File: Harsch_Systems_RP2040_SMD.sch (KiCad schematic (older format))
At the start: 53 parts, among them J1 Jack-DC, J3 Conn_01x08_Female, J4 Conn_01x08_Female, J5 Conn_01x04_Female, J6 Conn_01x06_Female, J7 USB_A, J8 DEBUG, SW1 SW_MEC_5E, U1 XC6210B332MR, U11 TPS56339DDC, U3 RP2040, U4 W25Q32JVSSIQ_TR, Y1 12MHz

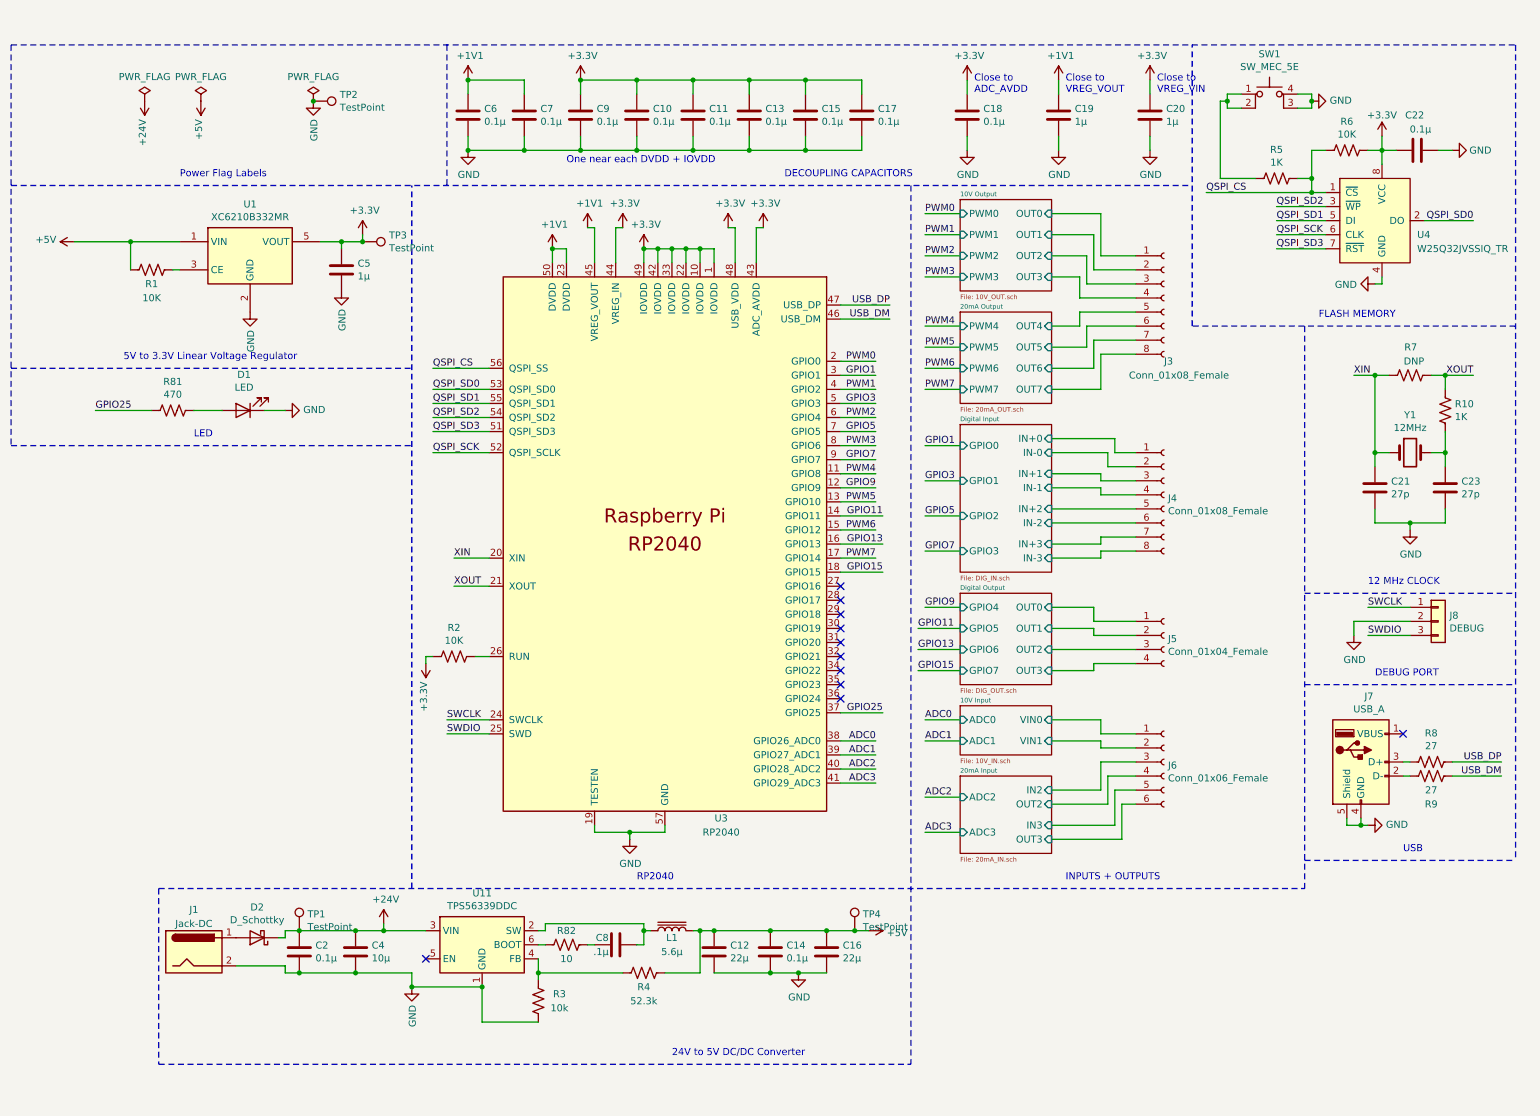
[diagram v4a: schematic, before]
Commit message: Everything but the 24V output is routed
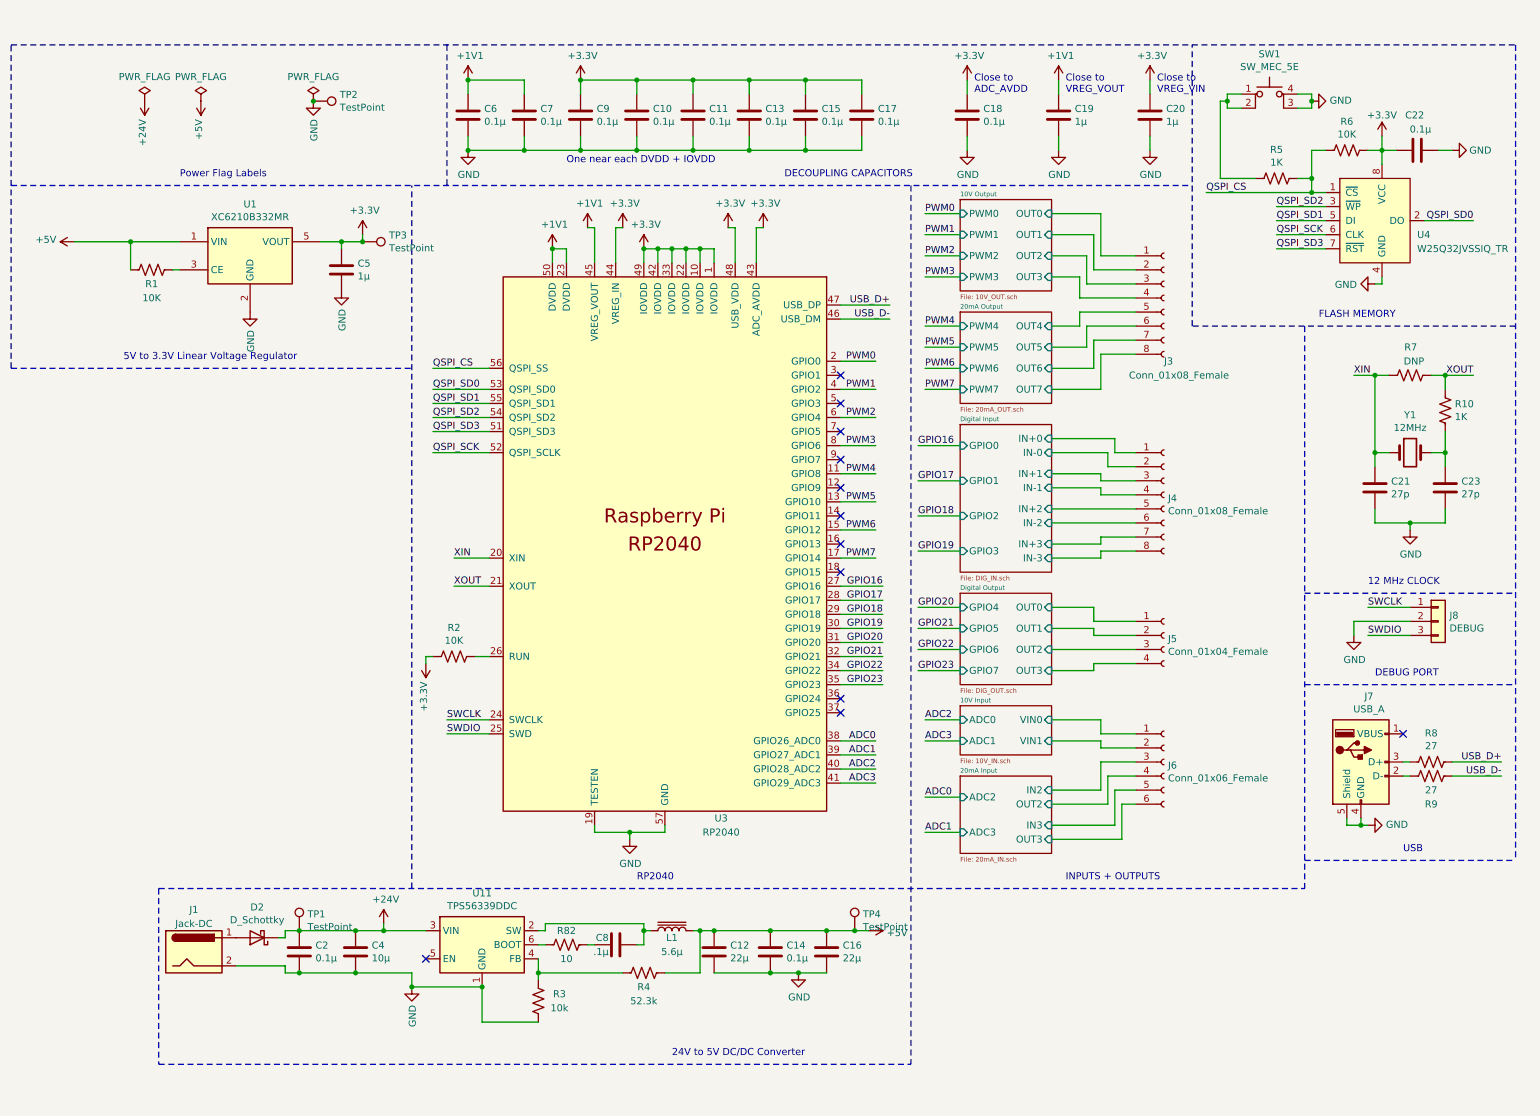
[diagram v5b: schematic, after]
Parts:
- removed D1: LED, LED_SMD:LED_0805_2012Metric, symbol Device:LED
- removed R81: 470, Resistor_SMD:R_0805_2012Metric, symbol Device:R_US
- C10, C11, C13, C15, C17, C6, C7, C9: footprint Capacitor_SMD:C_0402_1005Metric_Pad0.74x0.62mm_HandSolder -> Capacitor_SMD:C_0603_1608Metric
- C19, C20: footprint Capacitor_SMD:C_0805_2012Metric -> Capacitor_SMD:C_0603_1608Metric
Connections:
- net GPIO16: now reaches U3.27 (GPIO16)
- net GPIO17: now reaches U3.28 (GPIO17)
- net GPIO18: now reaches U3.29 (GPIO18)
- net GPIO19: now reaches U3.30 (GPIO19)
- net GPIO20: now reaches U3.31 (GPIO20)
- net GPIO21: now reaches U3.32 (GPIO21)
- net GPIO22: now reaches U3.34 (GPIO22)
- net GPIO23: now reaches U3.35 (GPIO23)
- net GPIO1: no longer names the net of U3.3 (GPIO1)
- net GPIO11: no longer names the net of U3.14 (GPIO11)
- net GPIO13: no longer names the net of U3.16 (GPIO13)
- net GPIO15: no longer names the net of U3.18 (GPIO15)
- net GPIO25: no longer names the net of U3.37 (GPIO25)
- net GPIO3: no longer names the net of U3.5 (GPIO3)
- net GPIO5: no longer names the net of U3.7 (GPIO5)
- net GPIO7: no longer names the net of U3.9 (GPIO7)
- net GPIO9: no longer names the net of U3.12 (GPIO9)
- net USB_DM renamed USB_D-
- net USB_DP renamed USB_D+
- no-connect marks 11 -> 12
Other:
- note removed: "LED"
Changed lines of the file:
@@
 F 0 "C9" H 4665 1046 50  0000 L CNN
 F 1 "0.1μ" H 4665 955 50  0000 L CNN
-F 2 "Capacitor_SMD:C_0402_1005Metric_Pad0.74x0.62mm_HandSolder" H 4588 850 50  0001 C CNN
+F 2 "Capacitor_SMD:C_0603_1608Metric" H 4588 850 50  0001 C CNN
 F 3 "~" H 4550 1000 50  0001 C CNN
 	1    4550 1000
@@
 F 0 "C10" H 5065 1046 50  0000 L CNN
 F 1 "0.1μ" H 5065 955 50  0000 L CNN
-F 2 "Capacitor_SMD:C_0402_1005Metric_Pad0.74x0.62mm_HandSolder" H 4988 850 50  0001 C CNN
+F 2 "Capacitor_SMD:C_0603_1608Metric" H 4988 850 50  0001 C CNN
 F 3 "~" H 4950 1000 50  0001 C CNN
 	1    4950 1000
@@
 F 0 "C11" H 5465 1046 50  0000 L CNN
 F 1 "0.1μ" H 5465 955 50  0000 L CNN
-F 2 "Capacitor_SMD:C_0402_1005Metric_Pad0.74x0.62mm_HandSolder" H 5388 850 50  0001 C CNN
+F 2 "Capacitor_SMD:C_0603_1608Metric" H 5388 850 50  0001 C CNN
 F 3 "~" H 5350 1000 50  0001 C CNN
 	1    5350 1000
@@
 F 0 "C13" H 5865 1046 50  0000 L CNN
 F 1 "0.1μ" H 5865 955 50  0000 L CNN
-F 2 "Capacitor_SMD:C_0402_1005Metric_Pad0.74x0.62mm_HandSolder" H 5788 850 50  0001 C CNN
+F 2 "Capacitor_SMD:C_0603_1608Metric" H 5788 850 50  0001 C CNN
 F 3 "~" H 5750 1000 50  0001 C CNN
 	1    5750 1000
@@
 F 0 "C15" H 6265 1046 50  0000 L CNN
 F 1 "0.1μ" H 6265 955 50  0000 L CNN
-F 2 "Capacitor_SMD:C_0402_1005Metric_Pad0.74x0.62mm_HandSolder" H 6188 850 50  0001 C CNN
+F 2 "Capacitor_SMD:C_0603_1608Metric" H 6188 850 50  0001 C CNN
 F 3 "~" H 6150 1000 50  0001 C CNN
 	1    6150 1000
@@
 F 0 "C17" H 6665 1046 50  0000 L CNN
 F 1 "0.1μ" H 6665 955 50  0000 L CNN
-F 2 "Capacitor_SMD:C_0402_1005Metric_Pad0.74x0.62mm_HandSolder" H 6588 850 50  0001 C CNN
+F 2 "Capacitor_SMD:C_0603_1608Metric" H 6588 850 50  0001 C CNN
 F 3 "~" H 6550 1000 50  0001 C CNN
 	1    6550 1000
@@
 Connection ~ 10100 6050
 Text Label 11100 5600 2    50   ~ 0
-USB_DP
+USB_D+
 Text Label 11100 5700 2    50   ~ 0
-USB_DM
+USB_D-
 $Comp
 L Device:R_US R8
@@
 	10750 5700 11100 5700
 Text Label 6750 2450 2    50   ~ 0
-USB_DM
+USB_D-
 Text Label 6750 2350 2    50   ~ 0
-USB_DP
+USB_D+
 Wire Wire Line
 	6400 2350 6750 2350
@@
 F 0 "C6" H 3865 1046 50  0000 L CNN
 F 1 "0.1μ" H 3865 955 50  0000 L CNN
-F 2 "Capacitor_SMD:C_0402_1005Metric_Pad0.74x0.62mm_HandSolder" H 3788 850 50  0001 C CNN
+F 2 "Capacitor_SMD:C_0603_1608Metric" H 3788 850 50  0001 C CNN
 F 3 "~" H 3750 1000 50  0001 C CNN
 	1    3750 1000
@@
 F 0 "C7" H 4265 1046 50  0000 L CNN
 F 1 "0.1μ" H 4265 955 50  0000 L CNN
-F 2 "Capacitor_SMD:C_0402_1005Metric_Pad0.74x0.62mm_HandSolder" H 4188 850 50  0001 C CNN
+F 2 "Capacitor_SMD:C_0603_1608Metric" H 4188 850 50  0001 C CNN
 F 3 "~" H 4150 1000 50  0001 C CNN
 	1    4150 1000
@@
 F 0 "C19" H 8065 1046 50  0000 L CNN
 F 1 "1μ" H 8065 955 50  0000 L CNN
-F 2 "Capacitor_SMD:C_0805_2012Metric" H 7988 850 50  0001 C CNN
+F 2 "Capacitor_SMD:C_0603_1608Metric" H 7988 850 50  0001 C CNN
 F 3 "~" H 7950 1000 50  0001 C CNN
 	1    7950 1000
@@
 F 0 "C20" H 8715 1046 50  0000 L CNN
 F 1 "1μ" H 8715 955 50  0000 L CNN
-F 2 "Capacitor_SMD:C_0805_2012Metric" H 8638 850 50  0001 C CNN
+F 2 "Capacitor_SMD:C_0603_1608Metric" H 8638 850 50  0001 C CNN
 F 3 "~" H 8600 1000 50  0001 C CNN
 	1    8600 1000
@@
 Wire Wire Line
 	8400 5900 8500 5900
-NoConn ~ 6400 4350
-NoConn ~ 6400 4450
-NoConn ~ 6400 4550
-NoConn ~ 6400 4650
-NoConn ~ 6400 4750
-NoConn ~ 6400 4850
-NoConn ~ 6400 4950
-NoConn ~ 6400 5050
 NoConn ~ 6400 5150
 $Comp
@@
 Wire Wire Line
 	6400 4150 6650 4150
-Text Label 6650 2850 2    50   ~ 0
-GPIO1
-Text Label 6650 3050 2    50   ~ 0
-GPIO3
-Text Label 6650 3250 2    50   ~ 0
-GPIO5
-Text Label 6650 3450 2    50   ~ 0
-GPIO7
-Text Label 6650 3650 2    50   ~ 0
-GPIO9
-Text Label 6700 3850 2    50   ~ 0
-GPIO11
-Text Label 6700 4050 2    50   ~ 0
-GPIO13
-Text Label 6700 4250 2    50   ~ 0
-GPIO15
-Wire Wire Line
-	6400 2850 6650 2850
-Wire Wire Line
-	6400 3050 6650 3050
-Wire Wire Line
-	6400 3250 6650 3250
-Wire Wire Line
-	6400 3450 6650 3450
-Wire Wire Line
-	6400 3850 6700 3850
-Wire Wire Line
-	6400 4050 6700 4050
-Wire Wire Line
-	6400 4250 6700 4250
-Wire Wire Line
-	6400 3650 6650 3650
+Text Label 6700 5050 2    50   ~ 0
+GPIO23
+Text Label 6700 4350 2    50   ~ 0
+GPIO16
+Text Label 6700 4450 2    50   ~ 0
+GPIO17
+Text Label 6700 4550 2    50   ~ 0
+GPIO18
+Text Label 6700 4650 2    50   ~ 0
+GPIO19
+Text Label 6700 4750 2    50   ~ 0
+GPIO20
+Text Label 6700 4850 2    50   ~ 0
+GPIO21
+Text Label 6700 4950 2    50   ~ 0
+GPIO22
+Wire Wire Line
+	6400 4750 6700 4750
+Wire Wire Line
+	6400 4850 6700 4850
+Wire Wire Line
+	6400 4950 6700 4950
 Text Label 7000 1700 0    50   ~ 0
 PWM0
@@
 Text Label 7000 2950 0    50   ~ 0
 PWM7
-Text Label 7000 3350 0    50   ~ 0
-GPIO1
-Text Label 7000 3600 0    50   ~ 0
-GPIO3
-Text Label 7000 3850 0    50   ~ 0
-GPIO5
-Text Label 7000 4100 0    50   ~ 0
-GPIO7
-Text Label 7000 4500 0    50   ~ 0
-GPIO9
+Text Label 6950 4950 0    50   ~ 0
+GPIO23
+Text Label 6950 3350 0    50   ~ 0
+GPIO16
+Text Label 6950 3600 0    50   ~ 0
+GPIO17
+Text Label 6950 3850 0    50   ~ 0
+GPIO18
+Text Label 6950 4100 0    50   ~ 0
+GPIO19
+Text Label 6950 4500 0    50   ~ 0
+GPIO20
 Text Label 6950 4650 0    50   ~ 0
-GPIO11
+GPIO21
 Text Label 6950 4800 0    50   ~ 0
-GPIO13
-Text Label 6950 4950 0    50   ~ 0
-GPIO15
+GPIO22
 Wire Wire Line
 	7000 1700 7250 1700
@@
 	7000 2950 7250 2950
 Wire Wire Line
-	7000 3350 7250 3350
-Wire Wire Line
-	7000 3600 7250 3600
-Wire Wire Line
-	7000 3850 7250 3850
-Wire Wire Line
-	7000 4100 7250 4100
-Wire Wire Line
-	7000 4500 7250 4500
+	6950 4500 7250 4500
 Wire Wire Line
 	6950 4650 7250 4650
 Wire Wire Line
 	6950 4800 7250 4800
-Wire Wire Line
-	6950 4950 7250 4950
 Text Label 6650 5450 2    50   ~ 0
 ADC0
@@
 Text Label 6650 5750 2    50   ~ 0
 ADC3
+Text Label 7000 5850 0    50   ~ 0
+ADC0
+Text Label 7000 6100 0    50   ~ 0
+ADC1
 Text Label 7000 5300 0    50   ~ 0
-ADC0
+ADC2
 Text Label 7000 5450 0    50   ~ 0
-ADC1
-Text Label 7000 5850 0    50   ~ 0
-ADC2
-Text Label 7000 6100 0    50   ~ 0
 ADC3
 Wire Wire Line
@@
 Text Notes 1300 2750 0    50   ~ 0
 5V to 3.3V Linear Voltage Regulator
-Wire Wire Line
-	6400 5250 6700 5250
-Text Label 6700 5250 2    50   ~ 0
-GPIO25
-$Comp
-L Device:LED D1
-U 1 1 61F17205
-P 2150 3100
-F 0 "D1" H 2143 2845 50  0000 C CNN
-F 1 "LED" H 2143 2936 50  0000 C CNN
-F 2 "LED_SMD:LED_0805_2012Metric" H 2150 3100 50  0001 C CNN
-F 3 "~" H 2150 3100 50  0001 C CNN
-	1    2150 3100
-	-1   0    0    1
-$EndComp
-$Comp
-L Device:R_US R81
-U 1 1 61F18BAC
-P 1650 3100
-F 0 "R81" V 1445 3100 50  0000 C CNN
-F 1 "470" V 1536 3100 50  0000 C CNN
-F 2 "Resistor_SMD:R_0805_2012Metric" V 1690 3090 50  0001 C CNN
-F 3 "~" H 1650 3100 50  0001 C CNN
-	1    1650 3100
-	0    1    1    0
-$EndComp
-Text Label 1100 3100 0    50   ~ 0
-GPIO25
-Wire Wire Line
-	1100 3100 1500 3100
-Wire Wire Line
-	1800 3100 2000 3100
-$Comp
-L power:GND #PWR05
-U 1 1 61F7823A
-P 2450 3100
-F 0 "#PWR05" H 2450 2850 50  0001 C CNN
-F 1 "GND" V 2455 2972 50  0000 R CNN
-F 2 "" H 2450 3100 50  0001 C CNN
-F 3 "" H 2450 3100 50  0001 C CNN
-	1    2450 3100
-	0    -1   -1   0
-$EndComp
-Wire Wire Line
-	2300 3100 2450 3100
-Wire Notes Line
-	500  3350 3350 3350
-Wire Notes Line
-	500  500  500  3350
-Text Notes 1800 3300 0    50   ~ 0
-LED
 $Comp
 L Connector:TestPoint TP4
@@
 Wire Wire Line
 	950  1900 1350 1900
+Wire Wire Line
+	7250 4950 6950 4950
+Wire Wire Line
+	7250 3350 6950 3350
+Wire Wire Line
+	7250 3600 6950 3600
+Wire Wire Line
+	7250 3850 6950 3850
+Wire Wire Line
+	7250 4100 6950 4100
+Wire Wire Line
+	6400 5050 6700 5050
+Wire Wire Line
+	6400 4350 6700 4350
+Wire Wire Line
+	6400 4450 6700 4450
+Wire Wire Line
+	6700 4550 6400 4550
+Wire Wire Line
+	6400 4650 6700 4650
+Wire Notes Line
+	500  2800 500  500
+NoConn ~ 6400 5250
+NoConn ~ 6400 4250
+NoConn ~ 6400 4050
+NoConn ~ 6400 3850
+NoConn ~ 6400 3650
+NoConn ~ 6400 3450
+NoConn ~ 6400 3250
+NoConn ~ 6400 3050
+NoConn ~ 6400 2850
 $EndSCHEMATC

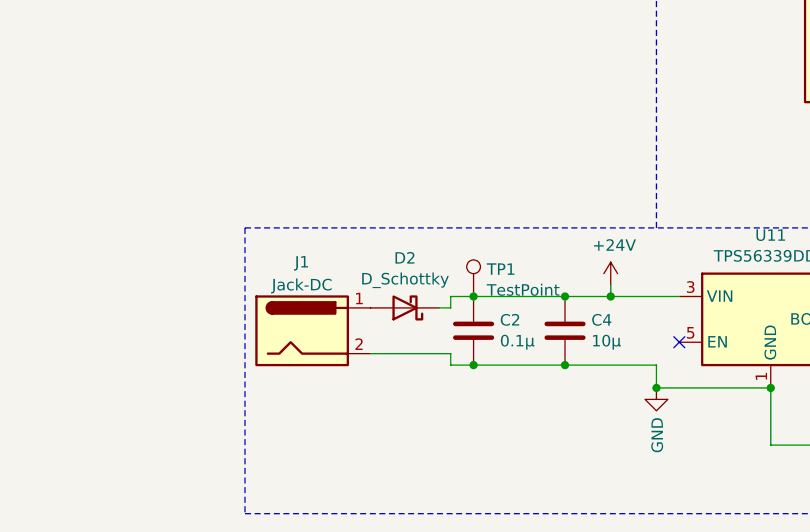
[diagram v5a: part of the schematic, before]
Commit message: Adjusted some tracks and vias for better heat dissipation
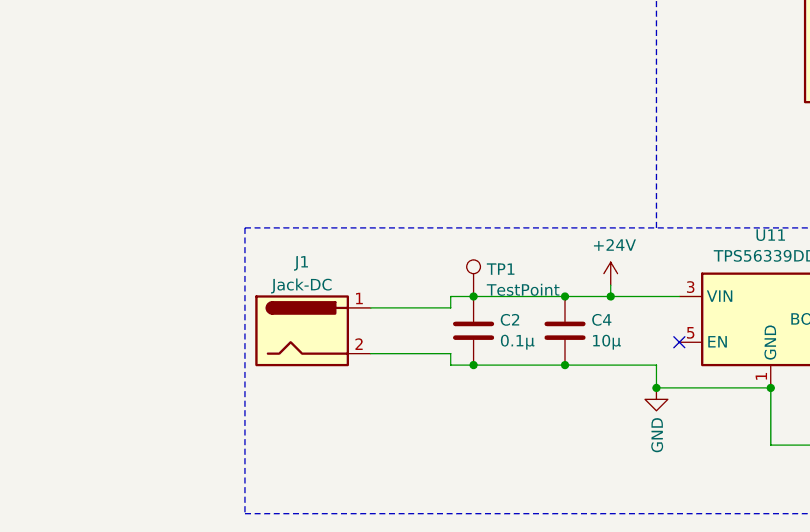
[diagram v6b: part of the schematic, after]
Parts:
- removed D2: D_Schottky, Diode_SMD:D_SOD-123, symbol Device:D_Schottky
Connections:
- net +24V: now also J1.1
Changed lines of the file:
@@
 $EndComp
-Wire Wire Line
-	2400 6850 2450 6850
 Wire Wire Line
 	2450 6850 2450 6800
@@
 	1    2200 2000
 	1    0    0    -1
-$EndComp
-$Comp
-L Device:D_Schottky D2
-U 1 1 619C10BE
-P 2250 6850
-F 0 "D2" H 2250 6633 50  0000 C CNN
-F 1 "D_Schottky" H 2250 6724 50  0000 C CNN
-F 2 "Diode_SMD:D_SOD-123" H 2250 6850 50  0001 C CNN
-F 3 "~" H 2250 6850 50  0001 C CNN
-	1    2250 6850
-	-1   0    0    1
 $EndComp
 Wire Wire Line
@@
 NoConn ~ 6400 3050
 NoConn ~ 6400 2850
+Wire Wire Line
+	2100 6850 2450 6850
 $EndSCHEMATC
